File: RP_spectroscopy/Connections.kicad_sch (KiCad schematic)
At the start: 29 parts, among them J1 Extension connector 1, J2 Extension connector 2, J3 Conn_Coaxial, J4 Conn_Coaxial, J5 Conn_Coaxial, J6 Conn_Coaxial, J7 Conn_01x04_MountingPin, J8 Conn_01x04_MountingPin, U4 MC78L05_SOT89, U5 L79L05_SOT89

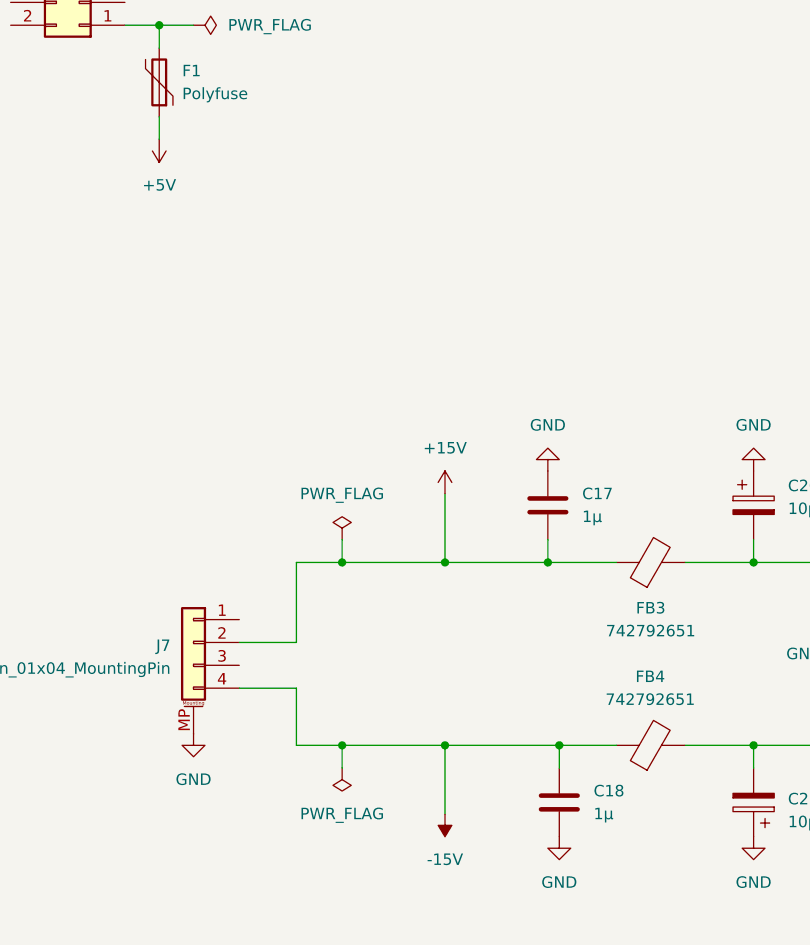
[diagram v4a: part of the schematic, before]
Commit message: Added the EMI filter in the +5V branch and added the powerline capacitors for the remaining opamps. Removed the tunable offset from the summator. Assigned right footprints and specs to all the components.
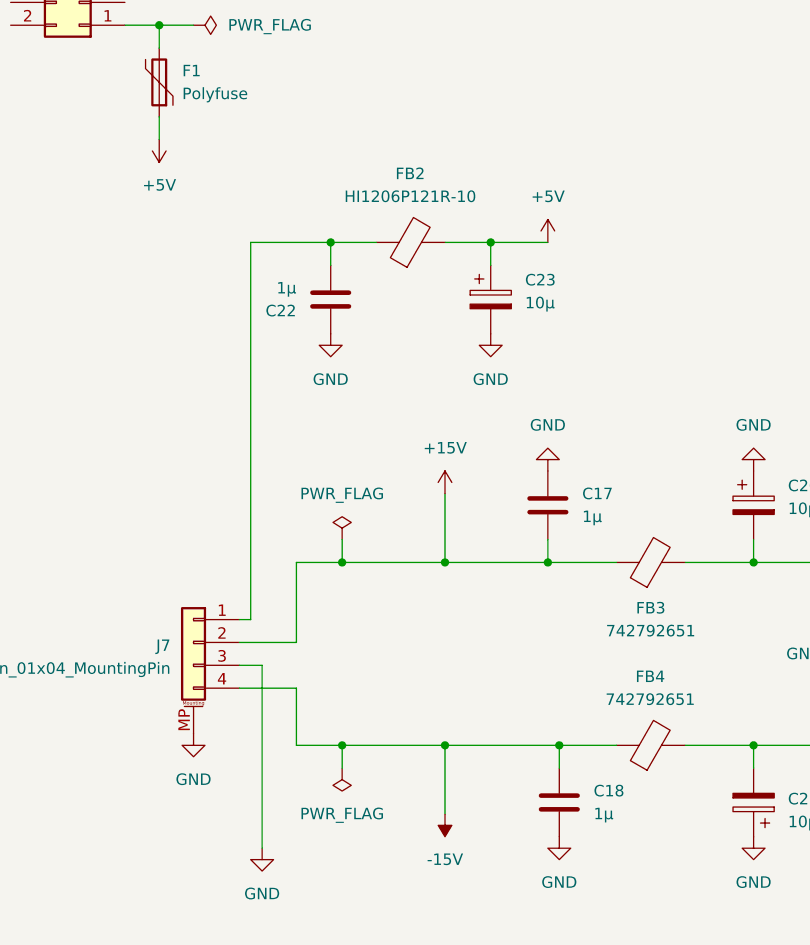
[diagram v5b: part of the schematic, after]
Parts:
- added C22: 1µ, Capacitor_SMD:C_0805_2012Metric_Pad1.18x1.45mm_HandSolder, symbol Device:C
- added C23: 10µ, Capacitor_SMD:CP_Elec_4x5.3, symbol Device:C_Polarized
- added FB2: HI1206P121R-10, symbol Device:FerriteBead
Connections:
- net +5V: now also C23.1, FB2.2
- net GND: now also J7.3 (Pin_3), C22.1, C23.2
- net at J7.1 (Pin_1): now also C22.2, FB2.1

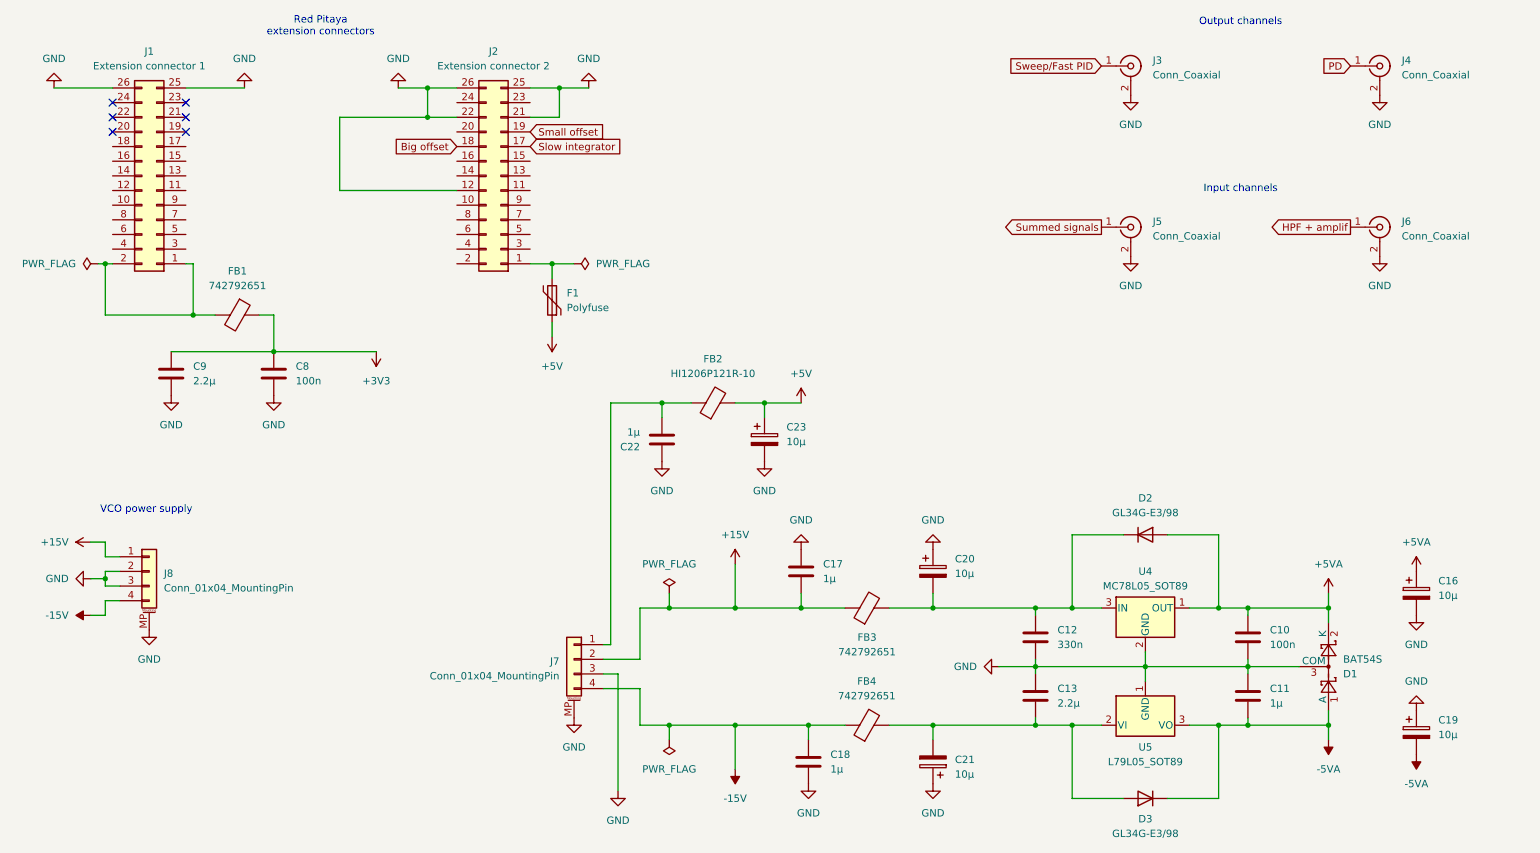
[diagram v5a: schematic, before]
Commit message: Changed the way of implementing the powerline capacitors in order to find them easily while creating the pcb. Started implementing the double Sallen-Key filter.
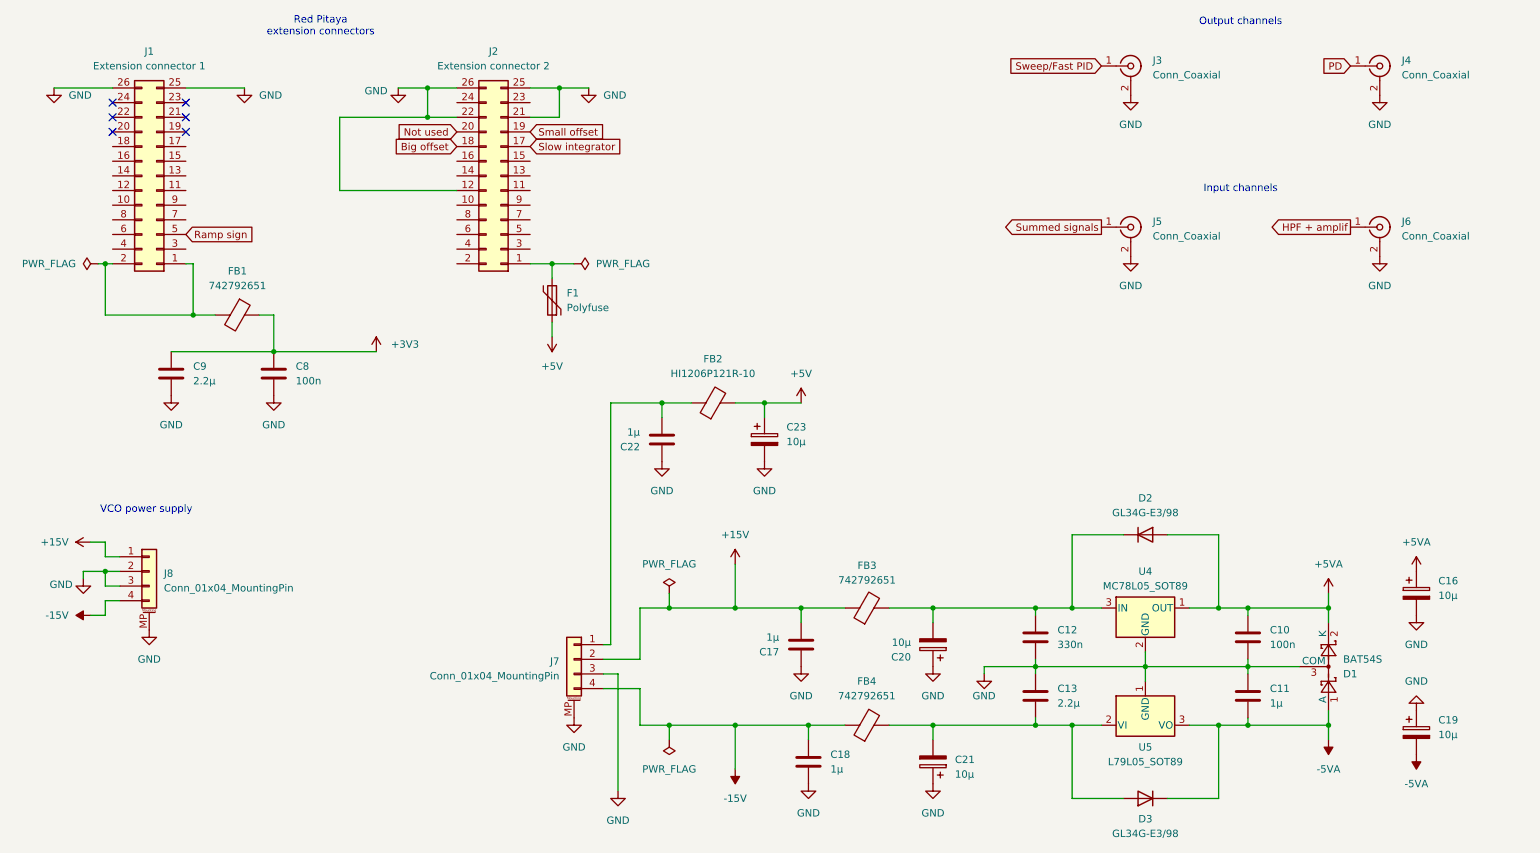
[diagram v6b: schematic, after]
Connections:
- net Ramp sign: now reaches J1.5 (Pin_5)
- net Not used: now reaches J2.20 (Pin_20)
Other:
- moved on the sheet: C17, C20

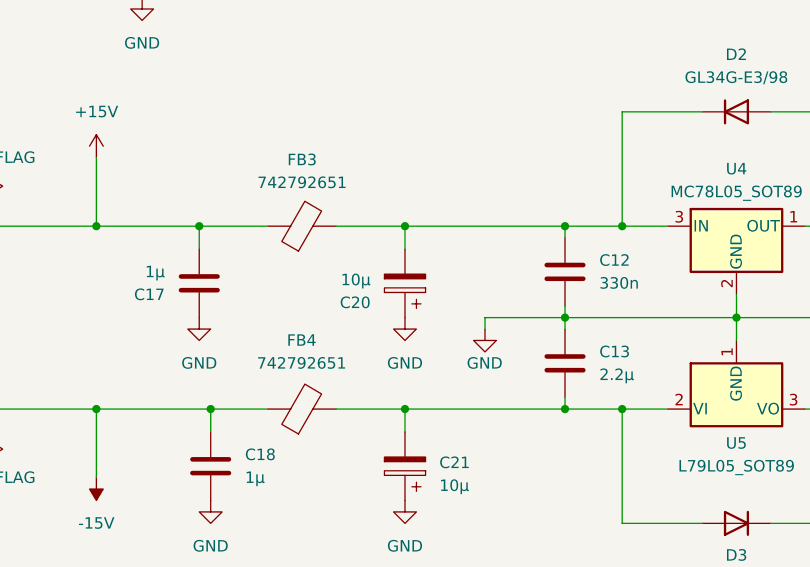
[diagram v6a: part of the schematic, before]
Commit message: Started to place all the components on the PCB. Simulated a bunch of filters.
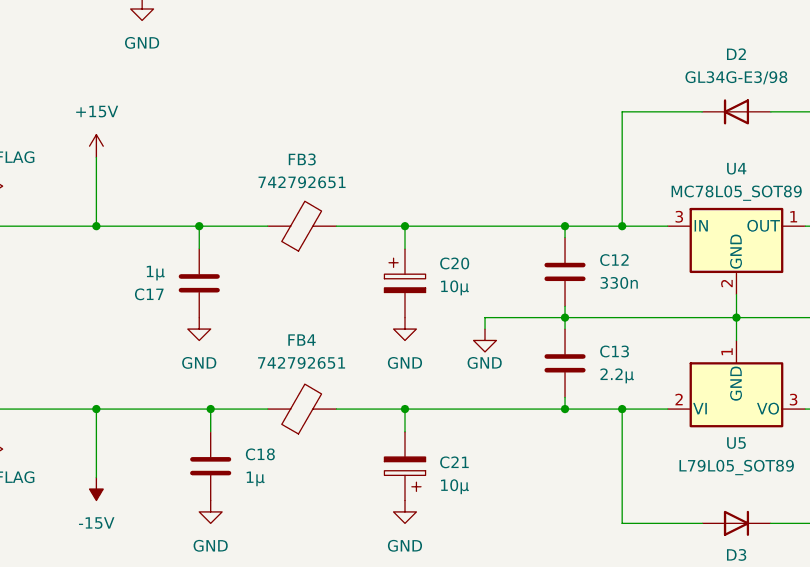
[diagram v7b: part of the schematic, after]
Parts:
- FB2: footprint (none) -> Inductor_SMD:L_1206_3216Metric_Pad1.22x1.90mm_HandSolder
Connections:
- net GND: now also C20.2; no longer C20.1
- net at C12.1, D2.1 (K), FB3.2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: now also C20.1; no longer C20.2
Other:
- moved on the sheet: C20
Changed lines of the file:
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@@
 			)
 		)
-		(property "Footprint" ""
+		(property "Footprint" "Inductor_SMD:L_1206_3216Metric_Pad1.22x1.90mm_HandSolder"
 			(at 143.51 88.138 90)
 			(effects
@@
 	(symbol
 		(lib_id "Device:C_Polarized")
-		(at 181.61 128.27 180)
+		(at 181.61 128.27 0)
 		(unit 1)
 		(exclude_from_sim no)
@@
 		(fields_autoplaced yes)
 		(property "Reference" "C20"
-			(at 177.8 130.4291 0)
+			(at 185.42 126.1109 0)
 			(effects
 				(font
@@
 		)
 		(property "Value" "10µ"
-			(at 177.8 127.8891 0)
+			(at 185.42 128.6509 0)
 			(effects
 				(font
@@
 		)
 		(property "Footprint" "Capacitor_SMD:CP_Elec_4x5.3"
-			(at 180.6448 124.46 0)
+			(at 182.5752 132.08 0)
 			(effects
 				(font

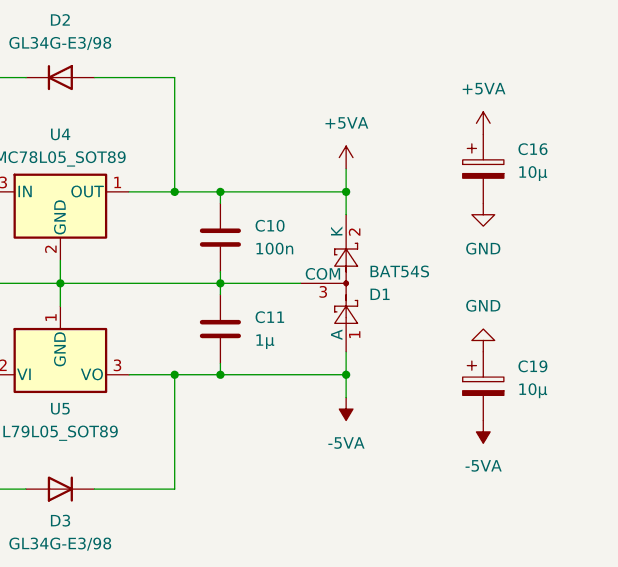
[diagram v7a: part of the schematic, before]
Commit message: Additional modifications of parameters for produciton and some footprints
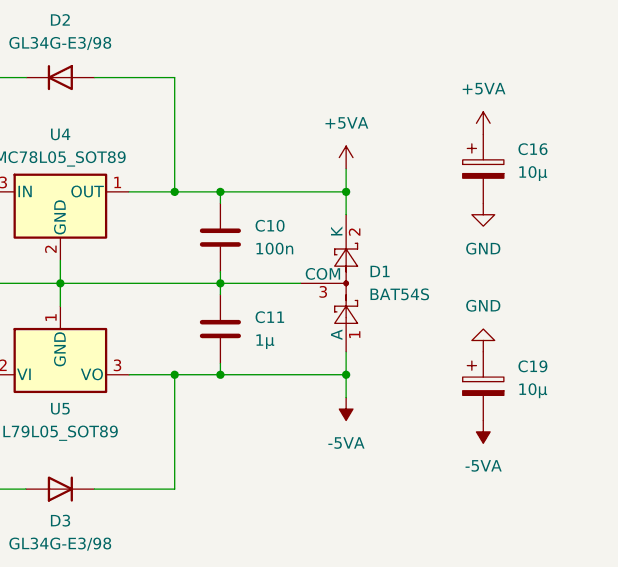
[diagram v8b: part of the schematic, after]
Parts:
- FB1: footprint Inductor_SMD:L_0805_2012Metric_Pad1.05x1.20mm_HandSolder -> Inductor_SMD:L_0603_1608Metric_Pad1.05x0.95mm_HandSolder
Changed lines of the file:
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@@
 		(fields_autoplaced yes)
 		(property "Reference" "D1"
-			(at 252.73 133.3501 90)
+			(at 252.73 130.8099 90)
 			(effects
 				(font
@@
 		)
 		(property "Value" "BAT54S"
-			(at 252.73 130.8101 90)
+			(at 252.73 133.3499 90)
 			(effects
 				(font
@@
 			)
 		)
-		(property "Footprint" "Inductor_SMD:L_0805_2012Metric_Pad1.05x1.20mm_HandSolder"
+		(property "Footprint" "Inductor_SMD:L_0603_1608Metric_Pad1.05x0.95mm_HandSolder"
 			(at 60.96 69.342 90)
 			(effects
